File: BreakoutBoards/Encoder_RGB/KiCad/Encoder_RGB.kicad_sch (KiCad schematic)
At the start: 6 parts, among them J1 Conn_01x08_Pin

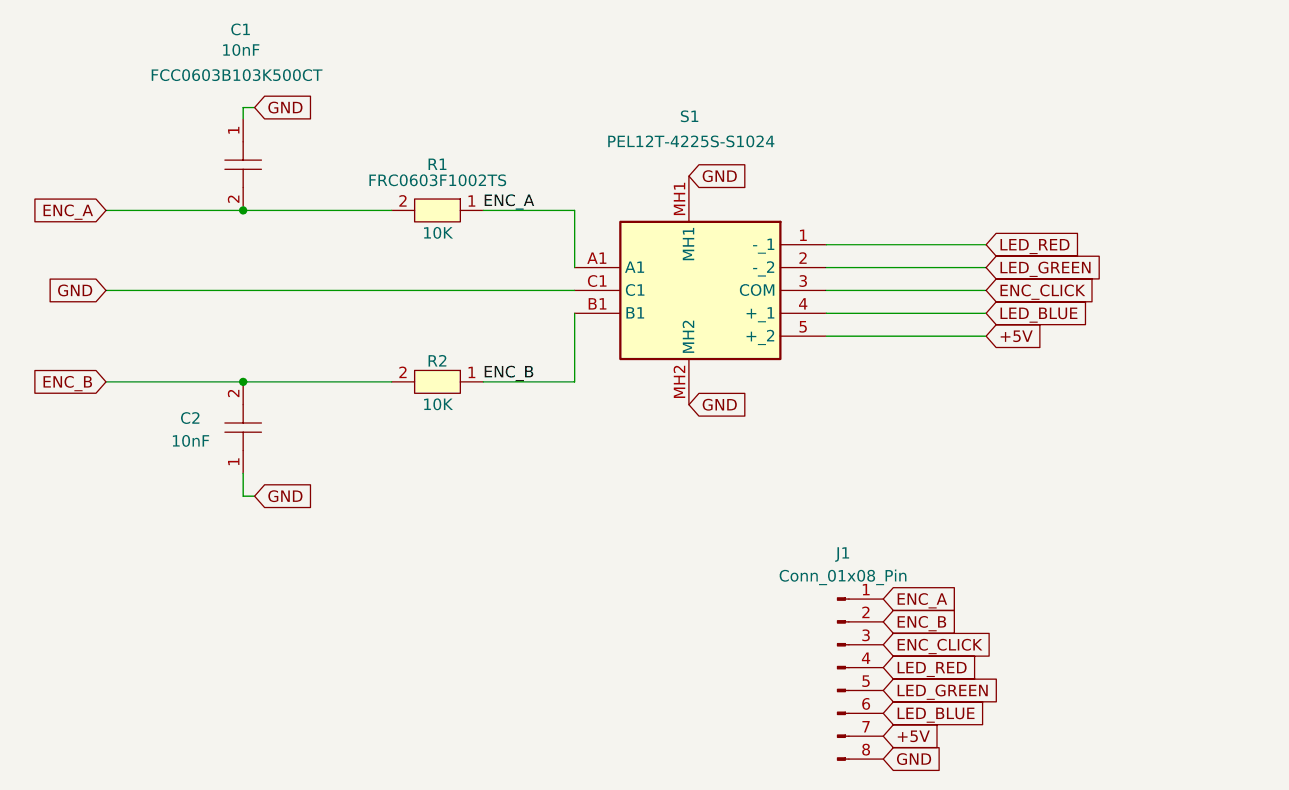
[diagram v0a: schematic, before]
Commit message: updated to Mk1 and sent for manufacturing
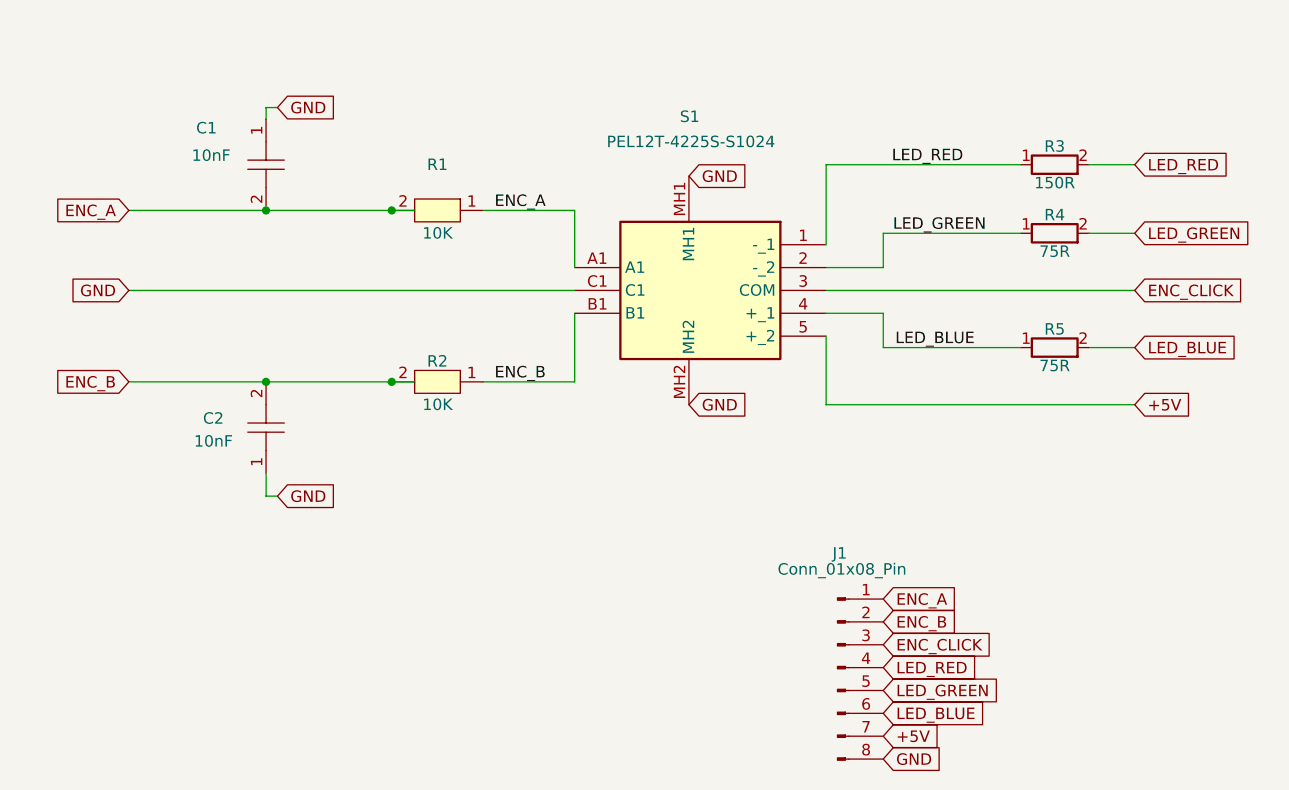
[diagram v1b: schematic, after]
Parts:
- added R3: 150R, clectric-diy:R0603, symbol Device:R
- added R4, R5: 75R, clectric-diy:R0603, symbol Device:R
- C1, C2: LCSC Part C5137477 -> (none)
- R1, R2: LCSC Part C2906982 -> (none)
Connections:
- net LED_BLUE: now also R5.1, R5.2
- net LED_GREEN: now also R4.1, R4.2
- net LED_RED: now also R3.1, R3.2
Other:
- title: Charge Encoder_RGB -> Charge Encoder w/ RGB LED
- moved on the sheet: C1, C2
